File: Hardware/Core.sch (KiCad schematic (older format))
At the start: 28 parts, among them U4 TM4C123GH6PGE, X2 12MHz, X3 32.768kHz

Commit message: Testing bottom side decoupling
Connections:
- net labels added: ADCS0, ADCS1, ADCS2, ADCS3, ADCS4, ADCS5, ADCS6, ADCS7, ADCS[0..7]
- wire segments 97 -> 105
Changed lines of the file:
@@
 Sheet 4 4
 Title ""
-Date "12 mar 2014"
+Date "15 mar 2014"
 Rev ""
 Comp ""
@@
 L TM4C123GH6PGE U4
 U 16 1 531F2A17
-P 3750 2750
-F 0 "U4" H 3750 3200 60  0000 C CNN
-F 1 "TM4C123GH6PGE" V 3550 2750 60  0000 C CNN
-F 2 "~" H 3750 2750 60  0000 C CNN
-F 3 "~" H 3750 2750 60  0000 C CNN
-	16   3750 2750
+P 4450 2750
+F 0 "U4" H 4450 3200 60  0000 C CNN
+F 1 "TM4C123GH6PGE" V 4250 2750 60  0000 C CNN
+F 2 "~" H 4450 2750 60  0000 C CNN
+F 3 "~" H 4450 2750 60  0000 C CNN
+	16   4450 2750
 	1    0    0    -1
 $EndComp
@@
 L TM4C123GH6PGE U4
 U 14 1 531F2A35
-P 3750 1750
-F 0 "U4" H 3750 2200 60  0000 C CNN
-F 1 "TM4C123GH6PGE" V 3550 1750 60  0000 C CNN
-F 2 "~" H 3750 1750 60  0000 C CNN
-F 3 "~" H 3750 1750 60  0000 C CNN
-	14   3750 1750
+P 4450 1750
+F 0 "U4" H 4450 2200 60  0000 C CNN
+F 1 "TM4C123GH6PGE" V 4250 1750 60  0000 C CNN
+F 2 "~" H 4450 1750 60  0000 C CNN
+F 3 "~" H 4450 1750 60  0000 C CNN
+	14   4450 1750
 	1    0    0    -1
 $EndComp
@@
 Text Notes 5000 7100 0    60   ~ 0
 Provision to short 3.3 to VMem
+Text Label 3300 2400 0    60   ~ 0
+ADCS0
+Text Label 3300 2500 0    60   ~ 0
+ADCS1
+Text Label 3300 2600 0    60   ~ 0
+ADCS2
+Text Label 3300 2700 0    60   ~ 0
+ADCS3
+Text Label 3300 2800 0    60   ~ 0
+ADCS4
+Text Label 3300 2900 0    60   ~ 0
+ADCS5
+Text Label 3300 3000 0    60   ~ 0
+ADCS6
+Text Label 3300 3100 0    60   ~ 0
+ADCS7
+Entry Bus Bus
+	3600 2400 3700 2500
+Entry Bus Bus
+	3600 2500 3700 2600
+Entry Bus Bus
+	3600 2600 3700 2700
+Entry Bus Bus
+	3600 2700 3700 2800
+Entry Bus Bus
+	3600 2800 3700 2900
+Entry Bus Bus
+	3600 2900 3700 3000
+Entry Bus Bus
+	3600 3000 3700 3100
+Entry Bus Bus
+	3600 3100 3700 3200
+Wire Bus Line
+	3700 2500 3700 3300
+Wire Bus Line
+	3700 3300 3800 3300
+Text HLabel 3800 3300 1    60   BiDi ~ 0
+ADCS[0..7]
+Wire Wire Line
+	3200 2400 3600 2400
+Wire Wire Line
+	3200 2500 3600 2500
+Wire Wire Line
+	3200 2600 3600 2600
+Wire Wire Line
+	3200 2700 3600 2700
+Wire Wire Line
+	3200 2800 3600 2800
+Wire Wire Line
+	3200 2900 3600 2900
+Wire Wire Line
+	3200 3000 3600 3000
+Wire Wire Line
+	3200 3100 3600 3100
 $EndSCHEMATC

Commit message: Add CAN transceiver
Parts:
- added C40: 0.1uF, CAPC1005-N, symbol C
- added R13: 10k, RESC1005-N, symbol R
- added R14: 120, RESC1005-N, symbol R
- added U5: SN65HVD233, symbol SN65HVD233
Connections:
- net labels added: CANEn, CANH, CANL, CANRX, CANTX, COM[0..7], D[0..7], EPS[0..7], PAY[0..5], USR[0..5]
- wire segments 105 -> 127
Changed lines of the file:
@@
 Sheet 4 4
 Title ""
-Date "15 mar 2014"
+Date "16 mar 2014"
 Rev ""
 Comp ""
@@
 Wire Wire Line
 	3200 3100 3600 3100
+Text HLabel 4500 3500 2    60   BiDi ~ 0
+EPS[0..7]
+Text HLabel 4500 3600 2    60   BiDi ~ 0
+COM[0..7]
+Text HLabel 4500 3700 2    60   BiDi ~ 0
+PAY[0..5]
+Text HLabel 4500 3800 2    60   BiDi ~ 0
+USR[0..5]
+Text HLabel 4500 3900 2    60   BiDi ~ 0
+D[0..7]
+$Comp
+L SN65HVD233 U5
+U 1 1 532516DD
+P 9000 6150
+F 0 "U5" H 9000 6400 60  0000 C CNN
+F 1 "SN65HVD233" H 9000 5900 60  0000 C CNN
+F 2 "" H 9000 6150 60  0000 C CNN
+F 3 "" H 9000 6150 60  0000 C CNN
+	1    9000 6150
+	1    0    0    -1
+$EndComp
+$Comp
+L R R14
+U 1 1 532516EC
+P 10000 6150
+F 0 "R14" H 10000 6250 50  0000 C CNN
+F 1 "120" H 10000 6150 50  0000 C CNN
+F 2 "RESC1005-N" H 10000 6150 60  0001 C CNN
+F 3 "~" H 10000 6150 60  0000 C CNN
+F 4 "W" H 10000 6050 50  0001 C CNN "Power"
+F 5 "%" H 10000 5950 50  0001 C CNN "Tolerance"
+	1    10000 6150
+	0    -1   -1   0
+$EndComp
+Text HLabel 10100 5800 2    60   BiDi ~ 0
+CANH
+Text HLabel 10100 6500 2    60   Input ~ 0
+CANL
+Wire Wire Line
+	9800 6500 10100 6500
+Wire Wire Line
+	9800 6500 9800 6200
+Wire Wire Line
+	9800 6200 9500 6200
+Wire Wire Line
+	9500 6100 9800 6100
+Wire Wire Line
+	9800 6100 9800 5800
+Wire Wire Line
+	9800 5800 10100 5800
+Wire Wire Line
+	10000 5900 10000 5800
+Connection ~ 10000 5800
+Wire Wire Line
+	10000 6400 10000 6500
+Connection ~ 10000 6500
+$Comp
+L R R13
+U 1 1 532519A6
+P 9250 5700
+F 0 "R13" H 9250 5800 50  0000 C CNN
+F 1 "10k" H 9250 5700 50  0000 C CNN
+F 2 "RESC1005-N" H 9250 5700 60  0001 C CNN
+F 3 "~" H 9250 5700 60  0000 C CNN
+F 4 "W" H 9250 5600 50  0001 C CNN "Power"
+F 5 "%" H 9250 5500 50  0001 C CNN "Tolerance"
+	1    9250 5700
+	1    0    0    -1
+$EndComp
+Wire Wire Line
+	9500 5700 9600 5700
+Wire Wire Line
+	9600 5700 9600 6000
+Wire Wire Line
+	9600 6000 9500 6000
+Text Label 8200 6000 2    60   ~ 0
+CANTX
+Text Label 8200 6300 2    60   ~ 0
+CANRX
+Wire Wire Line
+	8200 6300 8500 6300
+Wire Wire Line
+	8200 6000 8500 6000
+$Comp
+L +3.3V #PWR050
+U 1 1 53251C15
+P 8300 5800
+F 0 "#PWR050" H 8300 5760 30  0001 C CNN
+F 1 "+3.3V" H 8300 5910 30  0000 C CNN
+F 2 "" H 8300 5800 60  0000 C CNN
+F 3 "" H 8300 5800 60  0000 C CNN
+	1    8300 5800
+	1    0    0    -1
+$EndComp
+Wire Wire Line
+	8300 5800 8300 6200
+Wire Wire Line
+	8300 6200 8500 6200
+$Comp
+L GND #PWR051
+U 1 1 53251D1B
+P 8400 6400
+F 0 "#PWR051" H 8400 6400 30  0001 C CNN
+F 1 "GND" H 8400 6330 30  0001 C CNN
+F 2 "" H 8400 6400 60  0000 C CNN
+F 3 "" H 8400 6400 60  0000 C CNN
+	1    8400 6400
+	1    0    0    -1
+$EndComp
+Wire Wire Line
+	8400 6400 8400 6100
+Wire Wire Line
+	8400 6100 8500 6100
+$Comp
+L C C40
+U 1 1 53251DE8
+P 10600 6150
+F 0 "C40" H 10650 6300 60  0000 L CNN
+F 1 "0.1uF" H 10650 6000 60  0000 L CNN
+F 2 "CAPC1005-N" H 10600 6150 60  0001 C CNN
+F 3 "~" H 10600 6150 60  0000 C CNN
+F 4 "Samsung" H 10600 6150 60  0001 C CNN "MFR Name"
+F 5 "CL05A104MP5NNNC" H 10600 6150 60  0001 C CNN "MFR Part No"
+F 6 "1276-1443-1-ND" H 10600 6150 60  0001 C CNN "Distributor Part No"
+F 7 "10V" H 10550 6000 60  0001 R CNN "Voltage"
+F 8 "X5R" H 10550 6300 60  0001 R CNN "Dielectric"
+	1    10600 6150
+	1    0    0    -1
+$EndComp
+Text Label 8900 5700 2    60   ~ 0
+CANEn
+Wire Wire Line
+	8900 5700 9000 5700
+$Comp
+L GND #PWR052
+U 1 1 53251F94
+P 9600 6400
+F 0 "#PWR052" H 9600 6400 30  0001 C CNN
+F 1 "GND" H 9600 6330 30  0001 C CNN
+F 2 "" H 9600 6400 60  0000 C CNN
+F 3 "" H 9600 6400 60  0000 C CNN
+	1    9600 6400
+	1    0    0    -1
+$EndComp
+Wire Wire Line
+	9600 6400 9600 6300
+Wire Wire Line
+	9600 6300 9500 6300
+$Comp
+L GND #PWR053
+U 1 1 5325209F
+P 10600 6500
+F 0 "#PWR053" H 10600 6500 30  0001 C CNN
+F 1 "GND" H 10600 6430 30  0001 C CNN
+F 2 "" H 10600 6500 60  0000 C CNN
+F 3 "" H 10600 6500 60  0000 C CNN
+	1    10600 6500
+	1    0    0    -1
+$EndComp
+$Comp
+L +3.3V #PWR054
+U 1 1 532520AE
+P 10600 5800
+F 0 "#PWR054" H 10600 5760 30  0001 C CNN
+F 1 "+3.3V" H 10600 5910 30  0000 C CNN
+F 2 "" H 10600 5800 60  0000 C CNN
+F 3 "" H 10600 5800 60  0000 C CNN
+	1    10600 5800
+	1    0    0    -1
+$EndComp
+Wire Wire Line
+	10600 5800 10600 5900
+Wire Wire Line
+	10600 6400 10600 6500
 $EndSCHEMATC

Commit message: Switch to STM32F4 MCU
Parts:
- removed C39: 0.1uF, CAPC1005-N, symbol C
- removed U4: TM4C123GH6PGE, ~, symbol TM4C123GH6PGE
- added U4: STM32F407ZE, symbol STM32F407ZE
- C17, C18: value 0.1uF -> 2.2uF; Dielectric X5R -> D; Distributor Part No 1276-1443-1-ND -> (none); MFR Name Samsung -> (none); MFR Part No CL05A104MP5NNNC -> (none); Voltage 10V -> V
- C29, C30: value 3.3uF -> 0.1uF; Distributor Part No 445-8022-1-ND -> 1276-1443-1-ND; MFR Name TDK -> Samsung; MFR Part No C1005X5R1A335M050BC -> CL05A104MP5NNNC
- FB3: footprint INDC1005-N -> ~
- R12: value 1k -> 10k
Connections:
- net labels added: TRST
- net labels removed: ADCS0, ADCS1, ADCS2, ADCS3, ADCS4, ADCS5, ADCS6, ADCS7, GNDX
- wire segments 127 -> 89
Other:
- note removed: "Provision to short 3.3 to VMem"
- moved on the sheet: C32

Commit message: Clear core in prep for new MCU
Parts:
- removed C17, C18: 2.2uF, CAPC1005-N, symbol C
- removed C19, C20, C21, C22, C23, C24, C25, C26, C27, C28, C29, C30, C31, C37, C38, C40: 0.1uF, CAPC1005-N, symbol C
- removed C32: 3.3uF, CAPC1005-N, symbol C
- removed C33, C34, C35, C36: 10pF, CAPC1005-N, symbol C
- removed FB3: FERRITE, ~, symbol FERRITE
- removed R12, R13: 10k, RESC1005-N, symbol R
- removed R14: 120, RESC1005-N, symbol R
- removed U4: STM32F407ZE, symbol STM32F407ZE
- removed U5: SN65HVD233, symbol SN65HVD233
- removed X2: 12MHz, XTAL-4SMD-32X25, symbol CRYSTAL
- removed X3: 32.768kHz, XTAL-2SMD-32x15, symbol CRYSTAL
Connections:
- net labels removed: +3.3V, ADCS[0..7], CANEn, CANH, CANL, CANRX, CANTX, COM[0..7], D[0..7], EPS[0..7], GND, OSC0, OSC1, PAY[0..5], RST, TCK, TDI, TDO, TMS, TRST, USR[0..5], VMEM, XOSC0, XOSC1
- wire segments 89 -> 0
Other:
- note removed: "Reference: TI SPMA051"

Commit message: Rough pinout
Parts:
- added C? (x2): 10pF, CAPC1005-N, symbol C
- added U? (x11): STM32F427IIT6, symbol STM32F427I
- added U?: AS6C4008-55ST, symbol AS6C4008-55ST
- added U? (x2): S29AL016J-T, symbol S29AL016J-T
- added X?: 12MHz, XTAL-4SMD-32X25, symbol CRYSTAL
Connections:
- new net GND: C?.2, C?.2
- new net JTCK: U?.137 (PA14)
- new net JTDI: U?.138 (PA15)
- new net JTDO: U?.161 (PB3)
- new net JTMS: U?.124 (PA13)
- new net JTRST: U?.162 (PB4)
- new net M_A0: U?.16 (PF0), U?.20 (A0), U?.25 (A0), U?.25 (A0)
- new net M_A1: U?.17 (PF1), U?.19 (A1), U?.24 (A1), U?.24 (A1)
- new net M_A10: U?.31 (A10), U?.6 (A10), U?.6 (A10), U?.66 (PG0)
- new net M_A11: U?.1 (A11), U?.5 (A11), U?.5 (A11), U?.67 (PG1)
- new net M_A12: U?.106 (PG2), U?.12 (A12), U?.4 (A12), U?.4 (A12)
- new net M_A13: U?.107 (PG3), U?.3 (A13), U?.3 (A13), U?.4 (A13)
- new net M_A14: U?.108 (PG4), U?.11 (A14), U?.2 (A14), U?.2 (A14)
- new net M_A15: U?.1 (A15), U?.1 (A15), U?.109 (PG5), U?.7 (A15)
- new net M_A16: U?.10 (A16), U?.48 (A16), U?.48 (A16), U?.99 (PD11)
- new net M_A17: U?.100 (PD12), U?.17 (A17), U?.17 (A17), U?.6 (A17)
- new net M_A18: U?.101 (PD13), U?.16 (A18), U?.16 (A18), U?.9 (A18)
- new net M_A19: U?.2 (PE3), U?.9 (A19), U?.9 (A19)
- new net M_A2: U?.18 (A2), U?.18 (PF2), U?.23 (A2), U?.23 (A2)
- new net M_A20: U?.3 (PE4), U?.45 (D15), U?.45 (D15)
- new net M_A3: U?.17 (A3), U?.19 (PF3), U?.22 (A3), U?.22 (A3)
- new net M_A4: U?.16 (A4), U?.20 (PF4), U?.21 (A4), U?.21 (A4)
- new net M_A5: U?.15 (A5), U?.20 (A5), U?.20 (A5), U?.21 (PF5)
- new net M_A6: U?.14 (A6), U?.19 (A6), U?.19 (A6), U?.60 (PF12)
- new net M_A7: U?.13 (A7), U?.18 (A7), U?.18 (A7), U?.63 (PF13)
- new net M_A8: U?.3 (A8), U?.64 (PF14), U?.8 (A8), U?.8 (A8)
- new net M_A9: U?.2 (A9), U?.65 (PF15), U?.7 (A9), U?.7 (A9)
- new net M_D0: U?.104 (PD14), U?.21 (D0), U?.29 (D0), U?.29 (D0)
- new net M_D1: U?.105 (PD15), U?.22 (D1), U?.31 (D1), U?.31 (D1)
- new net M_D2: U?.142 (PD0), U?.23 (D2), U?.33 (D2), U?.33 (D2)
- new net M_D3: U?.143 (PD1), U?.25 (D3), U?.35 (D3), U?.35 (D3)
- new net M_D4: U?.26 (D4), U?.38 (D4), U?.38 (D4), U?.68 (PE7)
- new net M_D5: U?.27 (D5), U?.40 (D5), U?.40 (D5), U?.69 (PE8)
- new net M_D6: U?.28 (D6), U?.42 (D6), U?.42 (D6), U?.70 (PE9)
- new net M_D7: U?.29 (D7), U?.44 (D7), U?.44 (D7), U?.73 (PE10)
- new net M_RDY: U?.15 (RDY), U?.15 (RDY), U?.150 (PD6)
- new net OSC0: C?.1, U?.29 (PH0), X?.1
- new net OSC1: C?.1, U?.30 (PH1), X?.2
- new net SD_CK: U?.141 (PC12)
- new net SD_CMD: U?.144 (PD2)
- new net SD_D0: U?.117 (PC8)
- new net SD_D1: U?.118 (PC9)
- new net SD_D2: U?.139 (PC10)
- new net SD_D3: U?.140 (PC11)
- new net SOSC0: U?.9 (PC14)
- new net SOSC1: U?.10 (PC15)
- new net ~M_CE1: U?.151 (PD7), U?.30 (~CE)
- new net ~M_CE2: U?.152 (PG9), U?.26 (~CE)
- new net ~M_CE3: U?.153 (PG10), U?.26 (~CE)
- new net ~M_LE: U?.165 (PB7)
- new net ~M_OE: U?.146 (PD4), U?.28 (~OE), U?.28 (~OE), U?.32 (~OE)
- new net ~M_WE: U?.11 (~WE), U?.11 (~WE), U?.147 (PD5), U?.5 (~WE)

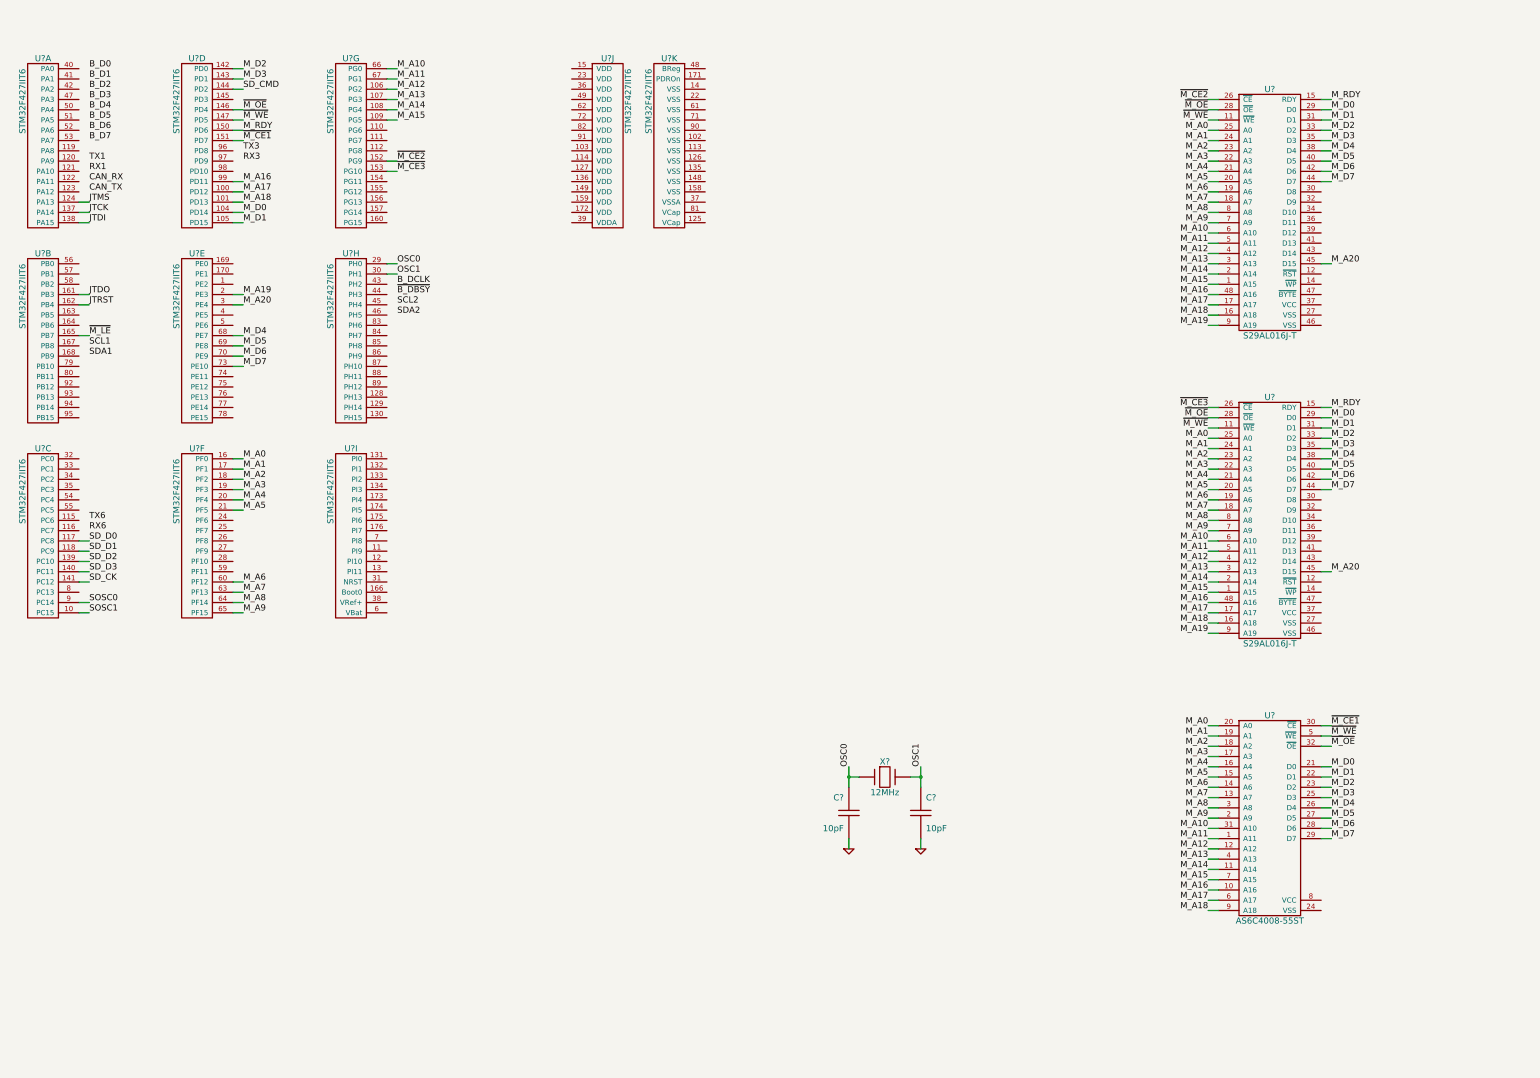
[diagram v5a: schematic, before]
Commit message: Add support components
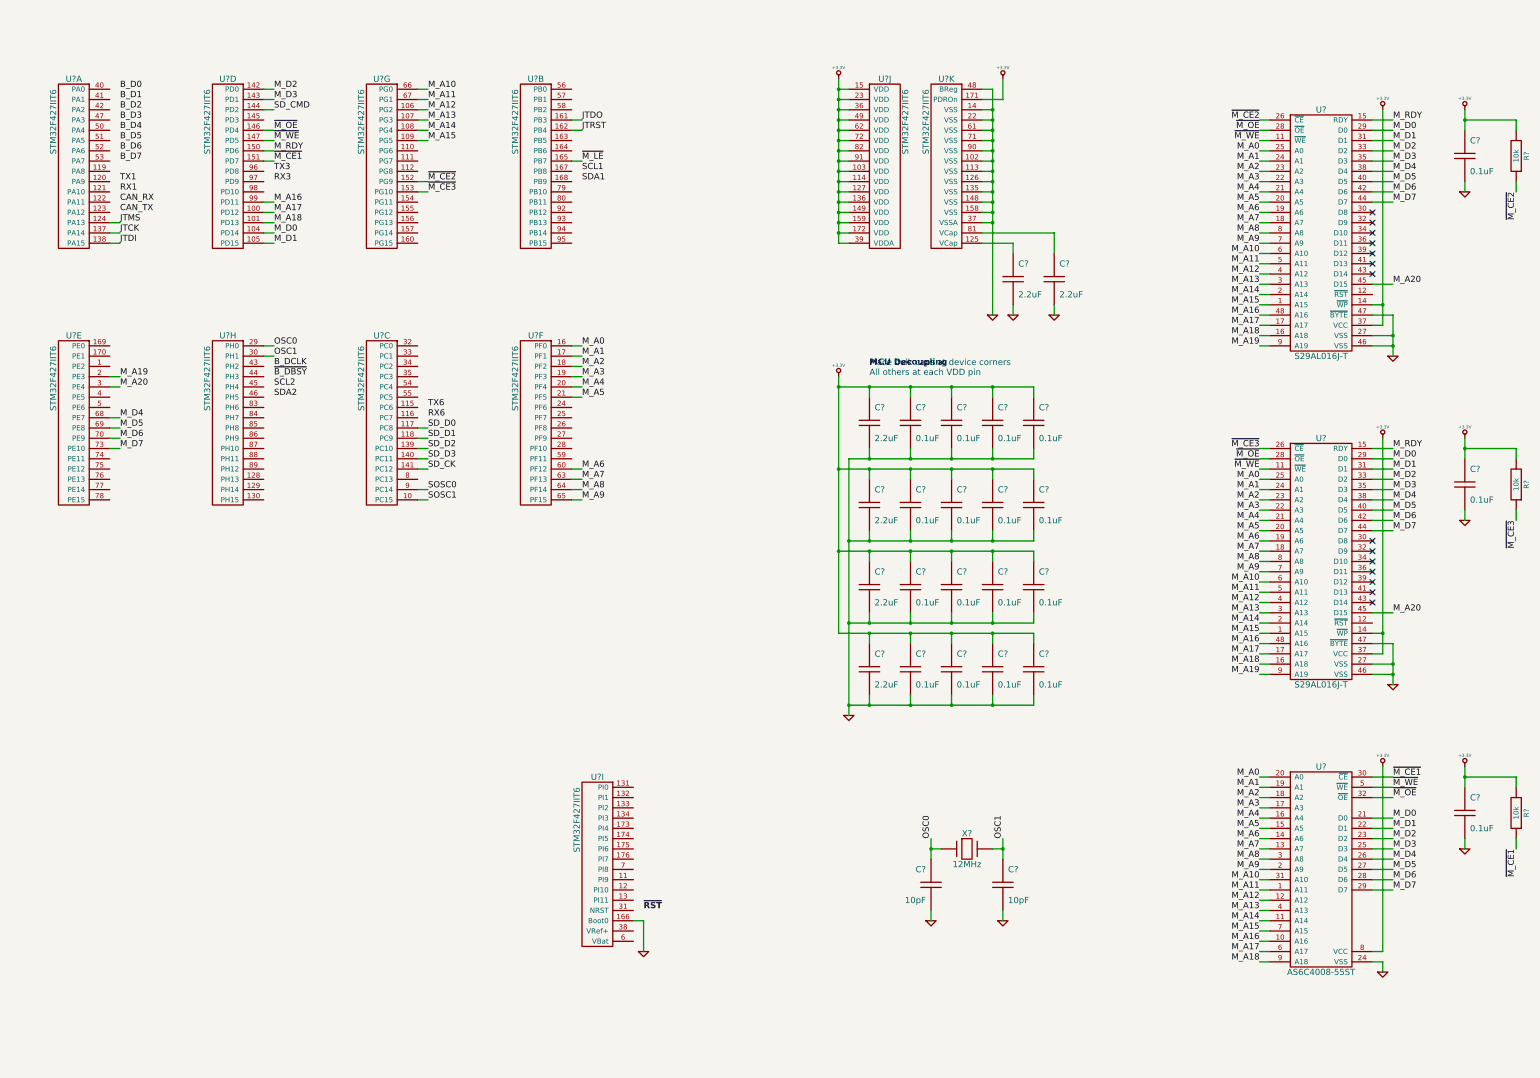
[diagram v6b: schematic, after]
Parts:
- added C? (x19): 0.1uF, CAPC1005-N, symbol C
- added C? (x6): 2.2uF, ~, symbol C
- added R? (x3): 10k, RESC1005-N, symbol R
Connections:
- net GND: now also U?.102 (VSS), U?.113 (VSS), U?.126 (VSS), U?.135 (VSS), U?.14 (VSS), U?.148 (VSS), U?.158 (VSS), U?.166 (Boot0), U?.22 (VSS), U?.24 (VSS), U?.27 (VSS), U?.27 (VSS), U?.37 (VSSA), U?.46 (VSS), U?.46 (VSS), U?.47 (~BYTE), U?.47 (~BYTE), U?.48 (BReg), U?.61 (VSS), U?.71 (VSS), U?.90 (VSS), C?.2, C?.2, C?.2, C?.2, C?.2, C?.2, C?.2, C?.2, C?.2, C?.2, C?.2, C?.2, C?.2, C?.2, C?.2, C?.2, C?.2, C?.2, C?.2, C?.2, C?.2, C?.2, C?.2, C?.2, C?.2
- net ~M_CE1: now also R?.1
- net ~M_CE2: now also R?.1
- net ~M_CE3: now also R?.1
- net +3.3V: now reaches U?.103 (VDD)
- net +3.3V: now also U?.114 (VDD), U?.127 (VDD), U?.136 (VDD), U?.14 (~WP), U?.14 (~WP), U?.149 (VDD), U?.15 (VDD), U?.159 (VDD), U?.171 (PDROn), U?.172 (VDD), U?.23 (VDD), U?.36 (VDD), U?.37 (VCC), U?.37 (VCC), U?.39 (VDDA), U?.49 (VDD), U?.62 (VDD), U?.72 (VDD), U?.8 (VCC), U?.82 (VDD), U?.91 (VDD), C?.1, C?.1, C?.1, C?.1, C?.1, C?.1, C?.1, C?.1, C?.1, C?.1, C?.1, C?.1, C?.1, C?.1, C?.1, C?.1, C?.1, C?.1, C?.1, C?.1, C?.1, C?.1, C?.1, R?.2, R?.2, R?.2
- net at U?.125 (VCap): now also C?.1
- net at U?.81 (VCap): now also C?.1
- no-connect marks 0 -> 14
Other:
- note added: "MCU Decoupling"
- note added: "Place bulk caps at device corners\nAll others at each VDD pin"
- moved on the sheet: C?, U?, U?A, U?B, U?C, U?D, U?E, U?F, U?G, U?H, U?I, U?J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
